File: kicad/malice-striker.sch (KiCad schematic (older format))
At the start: 66 parts, among them J1 Conn_01x02_Female, J2 Conn_01x02_Female, J3 Conn_01x02_Female, U1 TL072, U2 LT1054, U3 OP07, U4 TL072

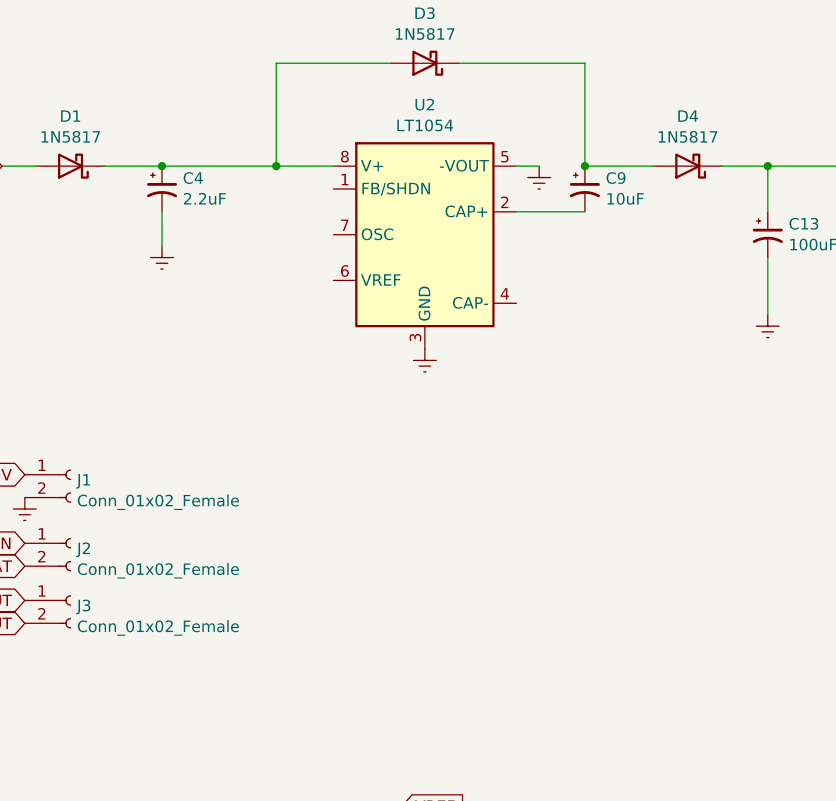
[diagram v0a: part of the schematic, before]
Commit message: added connections for LED and input/output grounds
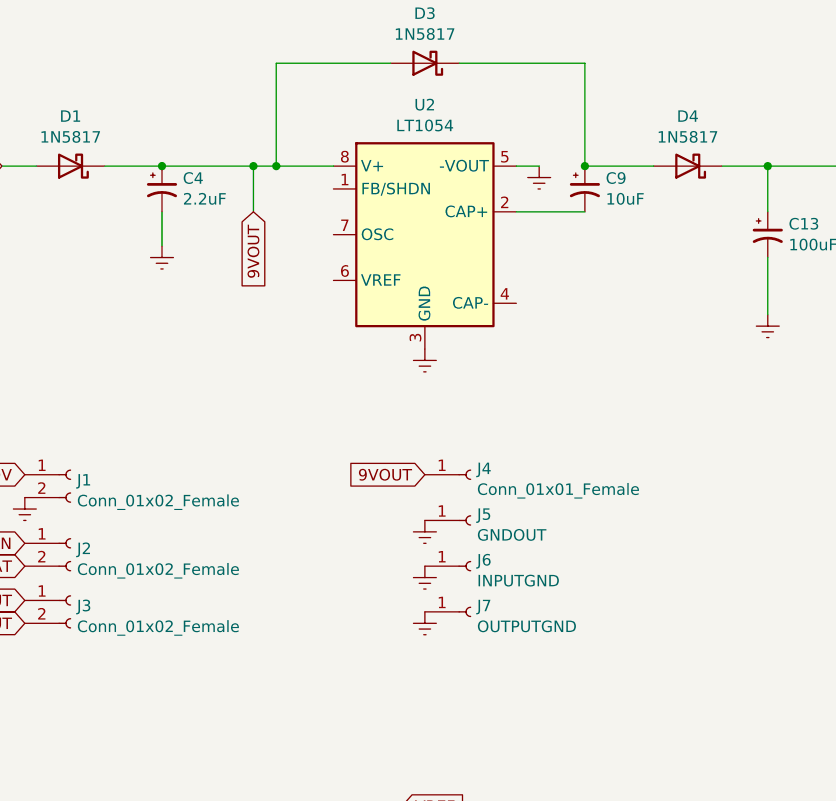
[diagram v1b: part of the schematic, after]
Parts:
- added J4: Conn_01x01_Female, Connector_PinSocket_2.54mm:PinSocket_1x01_P2.54mm_Vertical, symbol Connector:Conn_01x01_Female
- added J5: GNDOUT, Connector_PinSocket_2.54mm:PinSocket_1x01_P2.54mm_Vertical, symbol Connector:Conn_01x01_Female
- added J6: INPUTGND, Connector_PinSocket_2.54mm:PinSocket_1x01_P2.54mm_Vertical, symbol Connector:Conn_01x01_Female
- added J7: OUTPUTGND, Connector_PinSocket_2.54mm:PinSocket_1x01_P2.54mm_Vertical, symbol Connector:Conn_01x01_Female
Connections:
- net Earth: now also J5.1 (Pin_1), J6.1 (Pin_1), J7.1 (Pin_1)
- net 9VOUT: now reaches C4.1, D1.1 (K), D3.2 (A), U2.8 (V+)
- net 9VOUT: now also J4.1 (Pin_1)
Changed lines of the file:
@@
 $EndComp
 Wire Wire Line
-	3050 1750 3550 1750
+	3050 1750 3450 1750
 Connection ~ 3050 1750
 $Comp
@@
 Wire Wire Line
 	7850 1750 8300 1750
+$Comp
+L Connector:Conn_01x01_Female J4
+U 1 1 623FF7F6
+P 4400 3100
+F 0 "J4" H 4428 3126 50  0000 L CNN
+F 1 "Conn_01x01_Female" H 4428 3035 50  0000 L CNN
+F 2 "Connector_PinSocket_2.54mm:PinSocket_1x01_P2.54mm_Vertical" H 4400 3100 50  0001 C CNN
+F 3 "~" H 4400 3100 50  0001 C CNN
+	1    4400 3100
+	1    0    0    -1
+$EndComp
+Text GLabel 4200 3100 0    50   Input ~ 0
+9VOUT
+Text GLabel 3450 1950 3    50   Input ~ 0
+9VOUT
+Wire Wire Line
+	3450 1750 3450 1950
+Connection ~ 3450 1750
+Wire Wire Line
+	3450 1750 3550 1750
+$Comp
+L Connector:Conn_01x01_Female J5
+U 1 1 6240FC70
+P 4400 3300
+F 0 "J5" H 4428 3326 50  0000 L CNN
+F 1 "GNDOUT" H 4428 3235 50  0000 L CNN
+F 2 "Connector_PinSocket_2.54mm:PinSocket_1x01_P2.54mm_Vertical" H 4400 3300 50  0001 C CNN
+F 3 "~" H 4400 3300 50  0001 C CNN
+	1    4400 3300
+	1    0    0    -1
+$EndComp
+$Comp
+L power:Earth #PWR0113
+U 1 1 62417755
+P 4200 3300
+F 0 "#PWR0113" H 4200 3050 50  0001 C CNN
+F 1 "Earth" H 4200 3150 50  0001 C CNN
+F 2 "" H 4200 3300 50  0001 C CNN
+F 3 "~" H 4200 3300 50  0001 C CNN
+	1    4200 3300
+	1    0    0    -1
+$EndComp
+$Comp
+L Connector:Conn_01x01_Female J6
+U 1 1 624195D9
+P 4400 3500
+F 0 "J6" H 4428 3526 50  0000 L CNN
+F 1 "INPUTGND" H 4428 3435 50  0000 L CNN
+F 2 "Connector_PinSocket_2.54mm:PinSocket_1x01_P2.54mm_Vertical" H 4400 3500 50  0001 C CNN
+F 3 "~" H 4400 3500 50  0001 C CNN
+	1    4400 3500
+	1    0    0    -1
+$EndComp
+$Comp
+L power:Earth #PWR0114
+U 1 1 624195DF
+P 4200 3500
+F 0 "#PWR0114" H 4200 3250 50  0001 C CNN
+F 1 "Earth" H 4200 3350 50  0001 C CNN
+F 2 "" H 4200 3500 50  0001 C CNN
+F 3 "~" H 4200 3500 50  0001 C CNN
+	1    4200 3500
+	1    0    0    -1
+$EndComp
+$Comp
+L Connector:Conn_01x01_Female J7
+U 1 1 62421F90
+P 4400 3700
+F 0 "J7" H 4428 3726 50  0000 L CNN
+F 1 "OUTPUTGND" H 4428 3635 50  0000 L CNN
+F 2 "Connector_PinSocket_2.54mm:PinSocket_1x01_P2.54mm_Vertical" H 4400 3700 50  0001 C CNN
+F 3 "~" H 4400 3700 50  0001 C CNN
+	1    4400 3700
+	1    0    0    -1
+$EndComp
+$Comp
+L power:Earth #PWR0115
+U 1 1 62421F96
+P 4200 3700
+F 0 "#PWR0115" H 4200 3450 50  0001 C CNN
+F 1 "Earth" H 4200 3550 50  0001 C CNN
+F 2 "" H 4200 3700 50  0001 C CNN
+F 3 "~" H 4200 3700 50  0001 C CNN
+	1    4200 3700
+	1    0    0    -1
+$EndComp
 $EndSCHEMATC

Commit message: cleaned up PCB a bit
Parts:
- renumbered BASS1 to BASS, GAIN1 to GAIN, TREBLE1 to TREBLE, VOLUME1 to VOLUME
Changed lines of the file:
@@
 $EndComp
 $Comp
-L Device:R_POT_US BASS1
+L Device:R_POT_US BASS
 U 1 1 62379039
 P 9650 5150
-F 0 "BASS1" V 9445 5150 50  0000 C CNN
+F 0 "BASS" V 9445 5150 50  0000 C CNN
 F 1 "100k-A" V 9536 5150 50  0000 C CNN
 F 2 "clholm-kicad-lib:16MM_T.MOUNT" H 9650 5150 50  0001 C CNN
@@
 $EndComp
 $Comp
-L Device:R_POT_US TREBLE1
+L Device:R_POT_US TREBLE
 U 1 1 623B27C7
 P 9650 6250
-F 0 "TREBLE1" V 9445 6250 50  0000 C CNN
+F 0 "TREBLE" V 9445 6250 50  0000 C CNN
 F 1 "100k-A" V 9536 6250 50  0000 C CNN
 F 2 "clholm-kicad-lib:16MM_T.MOUNT" H 9650 6250 50  0001 C CNN
@@
 $EndComp
 $Comp
-L Device:R_POT_US VOLUME1
+L Device:R_POT_US VOLUME
 U 1 1 624250EE
 P 13100 5700
-F 0 "VOLUME1" H 13032 5746 50  0000 R CNN
+F 0 "VOLUME" H 13032 5746 50  0000 R CNN
 F 1 "100k-A" H 13032 5655 50  0000 R CNN
 F 2 "clholm-kicad-lib:16MM_T.MOUNT" H 13100 5700 50  0001 C CNN
@@
 $EndComp
 $Comp
-L Device:R_POT_US GAIN1
+L Device:R_POT_US GAIN
 U 1 1 622A90D0
 P 4950 6400
-F 0 "GAIN1" V 4837 6400 50  0000 C CNN
+F 0 "GAIN" V 4837 6400 50  0000 C CNN
 F 1 "1M-A" V 4746 6400 50  0000 C CNN
 F 2 "clholm-kicad-lib:16MM_T.MOUNT" H 4950 6400 50  0001 C CNN
